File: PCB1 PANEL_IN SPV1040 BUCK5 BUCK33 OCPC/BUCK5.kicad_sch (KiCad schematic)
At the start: 0 parts

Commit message: 2
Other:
- company: (none) -> TEAM ANANT
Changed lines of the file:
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@@
 	(generator_version "8.0")
 	(paper "A4")
+	(title_block
+		(company "TEAM ANANT")
+		(comment 1 "BITS PILANI")
+	)
 	(global_label "VBUS_IN"
 		(shape bidirectional)
@@
 				(hide yes)
 			)
+		)
+	)
+	(global_label "V_BUS_5V"
+		(shape input)
+		(at 52.07 68.58 180)
+		(fields_autoplaced yes)
+		(effects
+			(font
+				(size 1.27 1.27)
+			)
+			(justify right)
+		)
+		(property "Intersheetrefs" "${INTERSHEET_REFS}"
+			(at 39.9529 68.58 0)
+			(effects
+				(font
+					(size 1.27 1.27)
+				)
+				(justify right)
+				(hide yes)
+			)

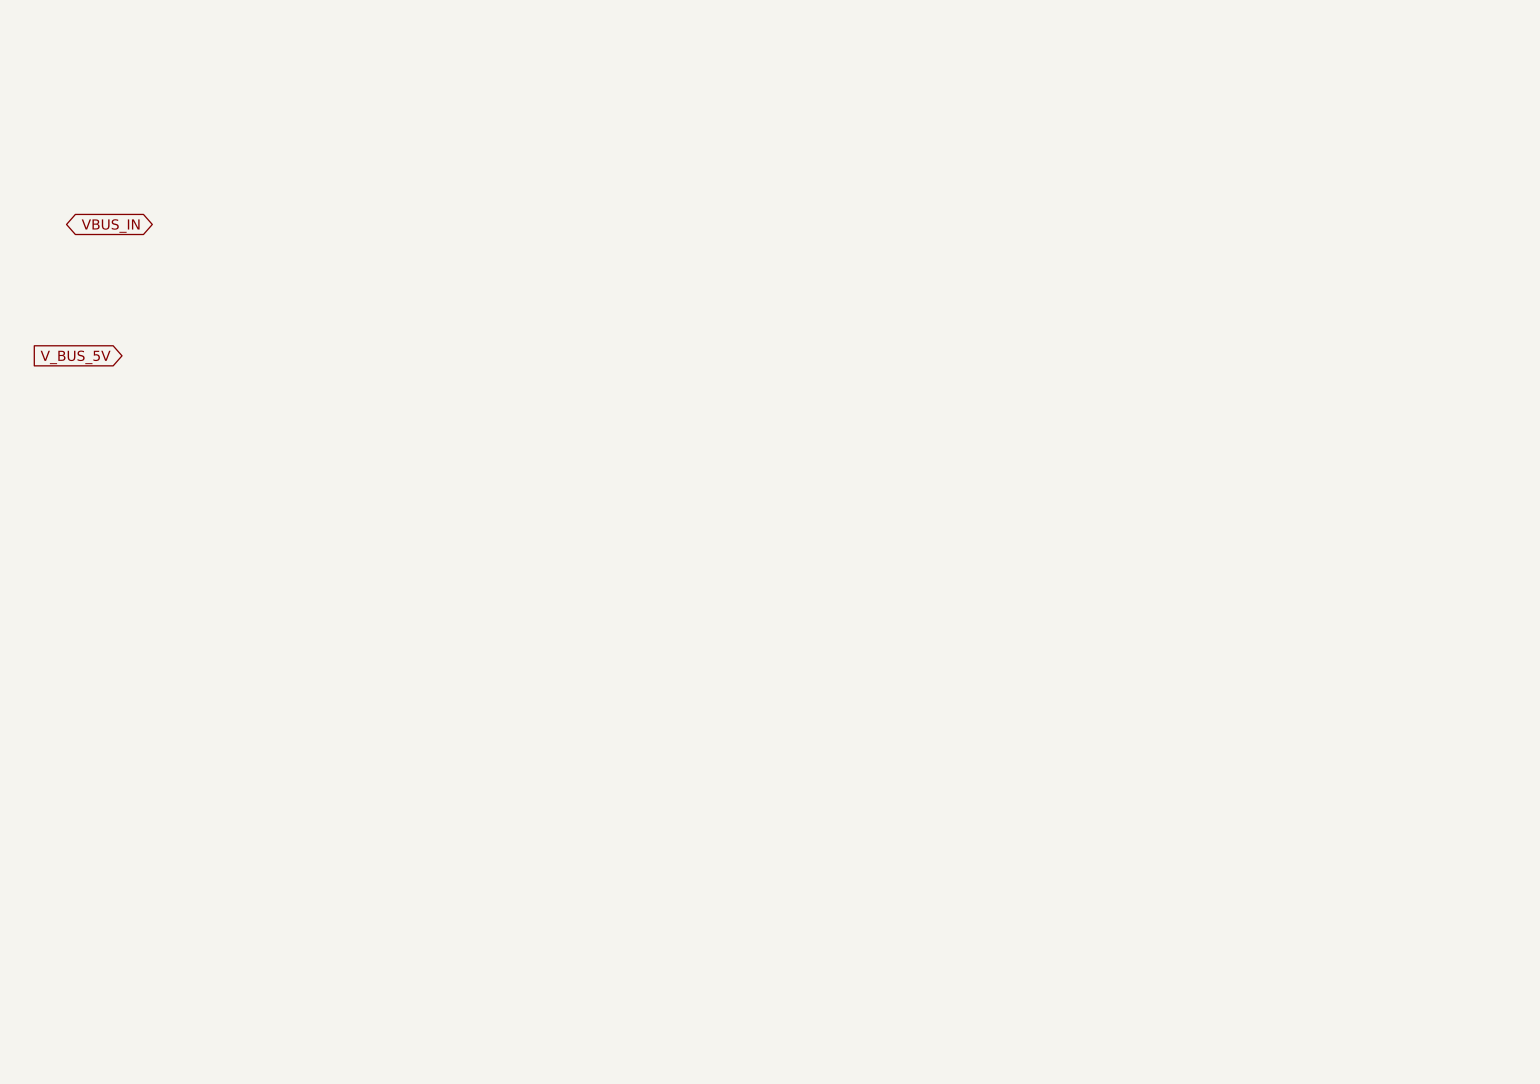
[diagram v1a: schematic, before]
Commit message: Changes
Added bucks from old work
and copied SPV
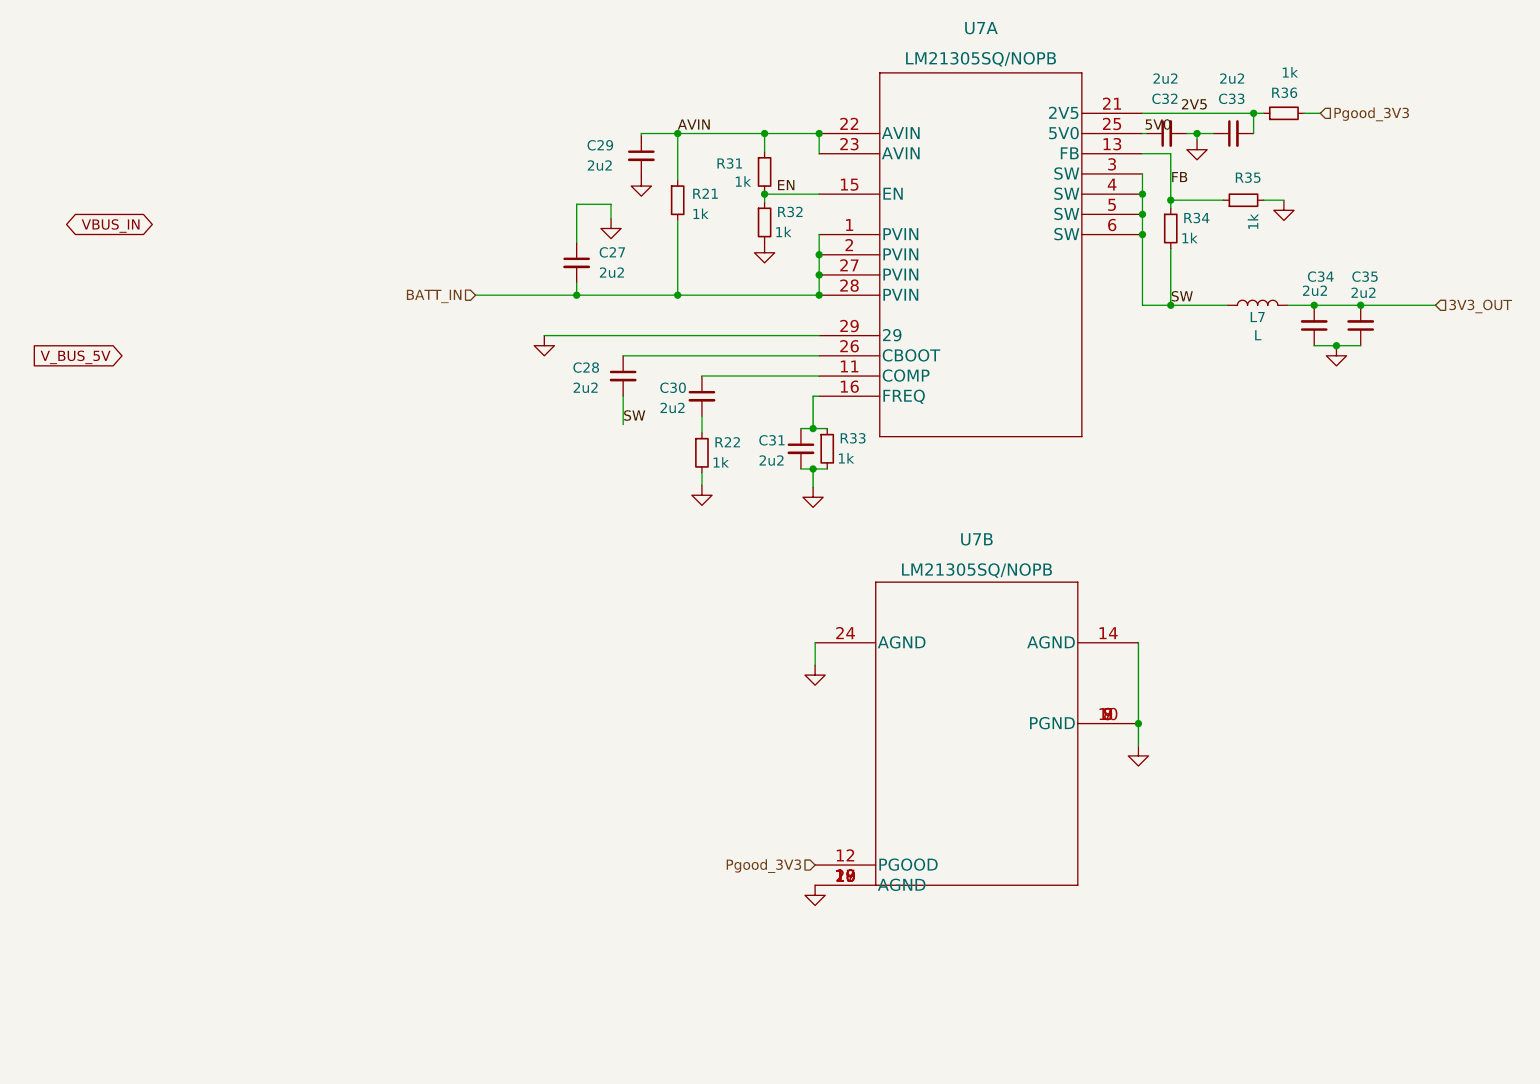
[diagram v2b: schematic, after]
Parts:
- added C27: 2u2, Capacitor_Tantalum_SMD:CP_EIA-7343-43_Kemet-X_Pad2.25x2.55mm_HandSolder, symbol Device:C_Small
- added C28, C29, C30, C31, C32, C33, C34, C35: 2u2, Capacitor_SMD:C_0603_1608Metric_Pad1.08x0.95mm_HandSolder, symbol Device:C_Small
- added L7: L, Inductor_SMD:L_6.3x6.3_H3, symbol Device:L
- added R21, R22, R31, R32, R33, R34, R35, R36: 1k, Resistor_SMD:R_0603_1608Metric_Pad0.98x0.95mm_HandSolder, symbol Device:R_Small
- added U7: LM21305SQ/NOPB, footprintLM21305:LM21305SQ&slash_NOPB, symbol 2023-03-29_16-01-02:LM21305SQ/NOPB
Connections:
- new net: C30.2, R22.1
- new net: C30.1, U7.11 (COMP)
- new net: C31.1, R33.1, U7.16 (FREQ)
- new net: C28.1, U7.26 (CBOOT)
- new net 2V5: C33.2, R36.1, U7.21 (2V5)
- new net 3V3_OUT: C34.2, C35.2, L7.2
- new net 5V0: C32.1, U7.25 (5V0)
- new net AVIN: C29.1, R21.1, R31.1, U7.22 (AVIN), U7.23 (AVIN)
- new net BATT_IN: C27.2, R21.2, U7.1 (PVIN), U7.2 (PVIN), U7.27 (PVIN), U7.28 (PVIN)
- new net EN: R31.2, R32.1, U7.15 (EN)
- new net FB: R34.1, R35.1, U7.13 (FB)
- new net GND: C27.1, C29.2, C31.2, C32.2, C33.1, C34.1, C35.1, R22.2, R32.2, R33.2, R35.2, U7.10 (PGND), U7.14 (AGND), U7.17 (AGND), U7.18 (AGND), U7.19 (AGND), U7.20 (AGND), U7.24 (AGND), U7.29, U7.7 (PGND), U7.8 (PGND), U7.9 (PGND)
- new net Pgood_3V3: R36.2, U7.12 (PGOOD)
- new net SW: C28.2, L7.1, R34.2, U7.3 (SW), U7.4 (SW), U7.5 (SW), U7.6 (SW)

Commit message: EDITS NTH
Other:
- note added: "MAKE THIS INTO 5V"
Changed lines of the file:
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@@
 	(paper "A4")
 	(title_block
+		(date "V1")
 		(company "TEAM ANANT")
 		(comment 1 "BITS PILANI")
@@
 		)
 	)
+	(text "MAKE THIS INTO 5V"
+		(exclude_from_sim no)
+		(at 162.56 152.908 0)
+		(effects
+			(font
+				(size 5.08 5.08)
+			)
+		)
+	)

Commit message: Relabeling according to standards
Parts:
- removed C27: 2u2, Capacitor_Tantalum_SMD:CP_EIA-7343-43_Kemet-X_Pad2.25x2.55mm_HandSolder, symbol Device:C_Small
- removed C28, C29, C30, C31, C32, C33, C34, C35: 2u2, Capacitor_SMD:C_0603_1608Metric_Pad1.08x0.95mm_HandSolder, symbol Device:C_Small
- removed L7: L, Inductor_SMD:L_6.3x6.3_H3, symbol Device:L
- removed R21, R22, R31, R32, R33, R34, R35, R36: 1k, Resistor_SMD:R_0603_1608Metric_Pad0.98x0.95mm_HandSolder, symbol Device:R_Small
- removed U7: LM21305SQ/NOPB, footprintLM21305:LM21305SQ&slash_NOPB, symbol 2023-03-29_16-01-02:LM21305SQ/NOPB
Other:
- note removed: "MAKE THIS INTO 5V"
